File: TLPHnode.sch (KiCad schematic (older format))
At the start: 0 parts

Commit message: Check-point: ESP-12E with two voltage regulators
Initial attempts at a layout show that I should use the ESP-12 footprint
to avoid pads for the extra connections on the end of the ESP-12E.

modified:   TLPHnode-cache.lib
modified:   TLPHnode.pro
modified:   TLPHnode.sch
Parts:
- added C1, C2, C3, C4, C5: 0.1 uF, Capacitors_SMD:C_0603, symbol C
- added P1: Bat, Pin_Headers:Pin_Header_Straight_1x02, symbol CONN_01X02
- added P2: CONN_01X06, FPConn:FPC6, symbol CONN_01X06
- added R1, R11, R5, R6, R7, R8, R9: 4.7k, Resistors_SMD:R_0603, symbol R
- added R10: 4.7, Resistors_SMD:R_0603, symbol R
- added R2, R3, R4: 10k, Resistors_SMD:R_0603, symbol R
- added SW1: Reset, Switches:SW-Mom-4p, symbol SW_Push
- added U1: NCP703, NCP703:TSOP-5, symbol NCP703
- added U2: LD39130S, LD39130S:FlipChip4, symbol LD39130S
- added U3: Si7006-A20, Si7006-A20:DFN6, symbol Si7006-A20
- added U4: ESP-12E, ESP8266:ESP-12E, symbol ESP-12E
- added U5: ISL29035, isl29035:ODFN, symbol ISL29035
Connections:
- net labels added: GND, I2C_SCL, I2C_SDA, PGM, RXD, TXD, VCC
- wire segments 0 -> 82
- no-connect marks 0 -> 10

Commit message: Use JST PH footprint for battery
modified:   TLPHnode.sch
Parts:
- P1: footprint Pin_Headers:Pin_Header_Straight_1x02 -> Connectors_JST:JST_PH_S2B-PH-SM4-TB_02x2.00mm_Angled
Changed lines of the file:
@@
 F 0 "P1" H 1178 2641 50  0000 L CNN
 F 1 "Bat" H 1178 2550 50  0000 L CNN
-F 2 "Pin_Headers:Pin_Header_Straight_1x02" H 1100 2600 50  0001 C CNN
+F 2 "Connectors_JST:JST_PH_S2B-PH-SM4-TB_02x2.00mm_Angled" H 1100 2600 50  0001 C CNN
 F 3 "" H 1100 2600 50  0000 C CNN
 	1    1100 2600

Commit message: Checkpoint before moving to kicad-rockingdlabs library
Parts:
- C1, C2: value 0.1 uF -> 1 uF
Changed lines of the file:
@@
 P 1400 3000
 F 0 "C1" H 1515 3046 50  0000 L CNN
-F 1 "0.1 uF" H 1515 2955 50  0000 L CNN
+F 1 "1 uF" H 1515 2955 50  0000 L CNN
 F 2 "Capacitors_SMD:C_0603" H 1438 2850 50  0001 C CNN
 F 3 "" H 1400 3000 50  0000 C CNN
@@
 P 3350 2750
 F 0 "C2" H 3400 2850 50  0000 L CNN
-F 1 "0.1 uF" H 3200 2650 50  0000 L CNN
+F 1 "1 uF" H 3200 2650 50  0000 L CNN
 F 2 "Capacitors_SMD:C_0603" H 3388 2600 50  0001 C CNN
 F 3 "" H 3350 2750 50  0000 C CNN
@@
 NoConn ~ 2450 2000
 Wire Wire Line
-	3250 1500 3600 1500
+	3600 1400 3600 2550
 Wire Wire Line
-	3600 1500 3600 2550
+	3200 1400 3600 1400
 $EndSCHEMATC

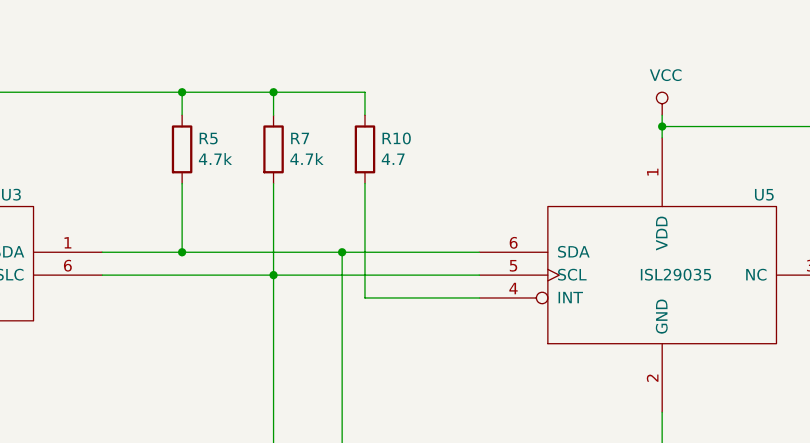
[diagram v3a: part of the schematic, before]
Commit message: Adjust paths for unified rockingdlabs library
On branch master
modified:   TLPHnode-cache.lib
modified:   TLPHnode.kicad_pcb
modified:   TLPHnode.pro
modified:   TLPHnode.sch
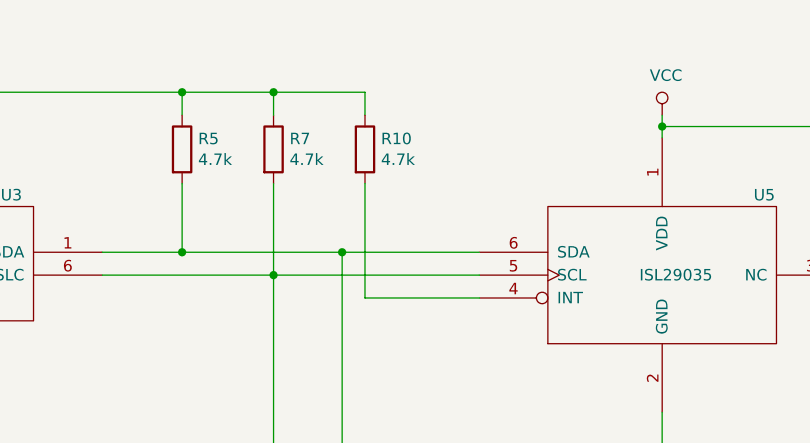
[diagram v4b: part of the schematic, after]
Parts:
- P2: footprint FPConn:FPC6 -> rockingdlabs:FPC-6-8.43x4.4x2.0mm_Pitch0.5mm
- R10: value 4.7 -> 4.7k
- SW1: footprint Switches:SW-Mom-4p -> rockingdlabs:ESwitch-SMD-4
- U1: footprint NCP703:TSOP-5 -> rockingdlabs:NCP703-TSOP-5
- U2: footprint LD39130S:FlipChip4 -> rockingdlabs:LD39130S-FlipChip-4
- U3: footprint Si7006-A20:DFN6 -> rockingdlabs:Si7006_A20-DFN-6
- U5: footprint isl29035:ODFN -> rockingdlabs:ISL29035-DFN-6-1.5x1.6mm_Pitch0.5mm
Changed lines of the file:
@@
 LIBS:valves
 LIBS:ESP8266
-LIBS:DS18B20
-LIBS:DS7505
-LIBS:ISL29035
-LIBS:net-tie
 LIBS:rockingdlabs
-LIBS:LPS25HB
-LIBS:NCP703
-LIBS:Si7006-A20
-LIBS:switches
-LIBS:LD39130SPUR
-LIBS:LD39130S
-LIBS:MAX884
 LIBS:TLPHnode-cache
 EELAYER 26 0
@@
 F 0 "U3" H 6450 2300 50  0000 R CNN
 F 1 "Si7006-A20" H 6200 2000 50  0000 R CNN
-F 2 "Si7006-A20:DFN6" H 6000 2000 50  0001 C CNN
+F 2 "rockingdlabs:Si7006_A20-DFN-6" H 6000 2000 50  0001 C CNN
 F 3 "DOCUMENTATION" H 6000 2000 50  0001 C CNN
 	1    6000 2000
@@
 F 0 "SW1" H 4700 4350 50  0000 C CNN
 F 1 "Reset" H 4750 4050 50  0000 C CNN
-F 2 "Switches:SW-Mom-4p" H 4750 4350 50  0001 C CNN
+F 2 "rockingdlabs:ESwitch-SMD-4" H 4750 4350 50  0001 C CNN
 F 3 "" H 4750 4350 50  0000 C CNN
 	1    4750 4150
@@
 F 0 "P2" H 4078 6391 50  0000 L CNN
 F 1 "CONN_01X06" H 4078 6300 50  0000 L CNN
-F 2 "FPConn:FPC6" H 4000 6350 50  0001 C CNN
+F 2 "rockingdlabs:FPC-6-8.43x4.4x2.0mm_Pitch0.5mm" H 4000 6350 50  0001 C CNN
 F 3 "" H 4000 6350 50  0000 C CNN
 	1    4000 6350
@@
 P 7950 1500
 F 0 "R10" H 8020 1546 50  0000 L CNN
-F 1 "4.7" H 8020 1455 50  0000 L CNN
+F 1 "4.7k" H 8020 1455 50  0000 L CNN
 F 2 "Resistors_SMD:R_0603" V 7880 1500 50  0001 C CNN
 F 3 "" H 7950 1500 50  0000 C CNN
@@
 F 0 "U5" H 9650 2400 50  0000 L CNN
 F 1 "ISL29035" H 9150 2050 50  0000 L CNN
-F 2 "isl29035:ODFN" H 8550 1600 50  0001 C CNN
+F 2 "rockingdlabs:ISL29035-DFN-6-1.5x1.6mm_Pitch0.5mm" H 8550 1600 50  0001 C CNN
 F 3 "" H 8550 1500 50  0001 C CNN
 	1    9250 2050
@@
 F 0 "U2" H 2800 2900 50  0000 C CNN
 F 1 "LD39130S" H 2400 2650 50  0000 C CNN
-F 2 "LD39130S:FlipChip4" H 2400 2600 50  0001 C CNN
+F 2 "rockingdlabs:LD39130S-FlipChip-4" H 2400 2600 50  0001 C CNN
 F 3 "DOCUMENTATION" H 2400 2600 50  0001 C CNN
 	1    2400 2600
@@
 F 0 "U1" H 2400 1865 50  0000 C CNN
 F 1 "NCP703" H 2400 1774 50  0000 C CNN
-F 2 "NCP703:TSOP-5" H 2400 1450 50  0001 C CNN
+F 2 "rockingdlabs:NCP703-TSOP-5" H 2400 1450 50  0001 C CNN
 F 3 "DOCUMENTATION" H 2400 1450 50  0001 C CNN
 	1    2400 1450
